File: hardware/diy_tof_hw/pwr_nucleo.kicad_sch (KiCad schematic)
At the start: 19 parts, among them IC1 TDC7200PWR, IC2 TDC7200PWR, J1 Conn_01x02_Pin, J2 Conn_01x03_Pin, J3 Conn_01x02_Pin, U1 NUCLEO-F042K6, X1 SG-5032CAN

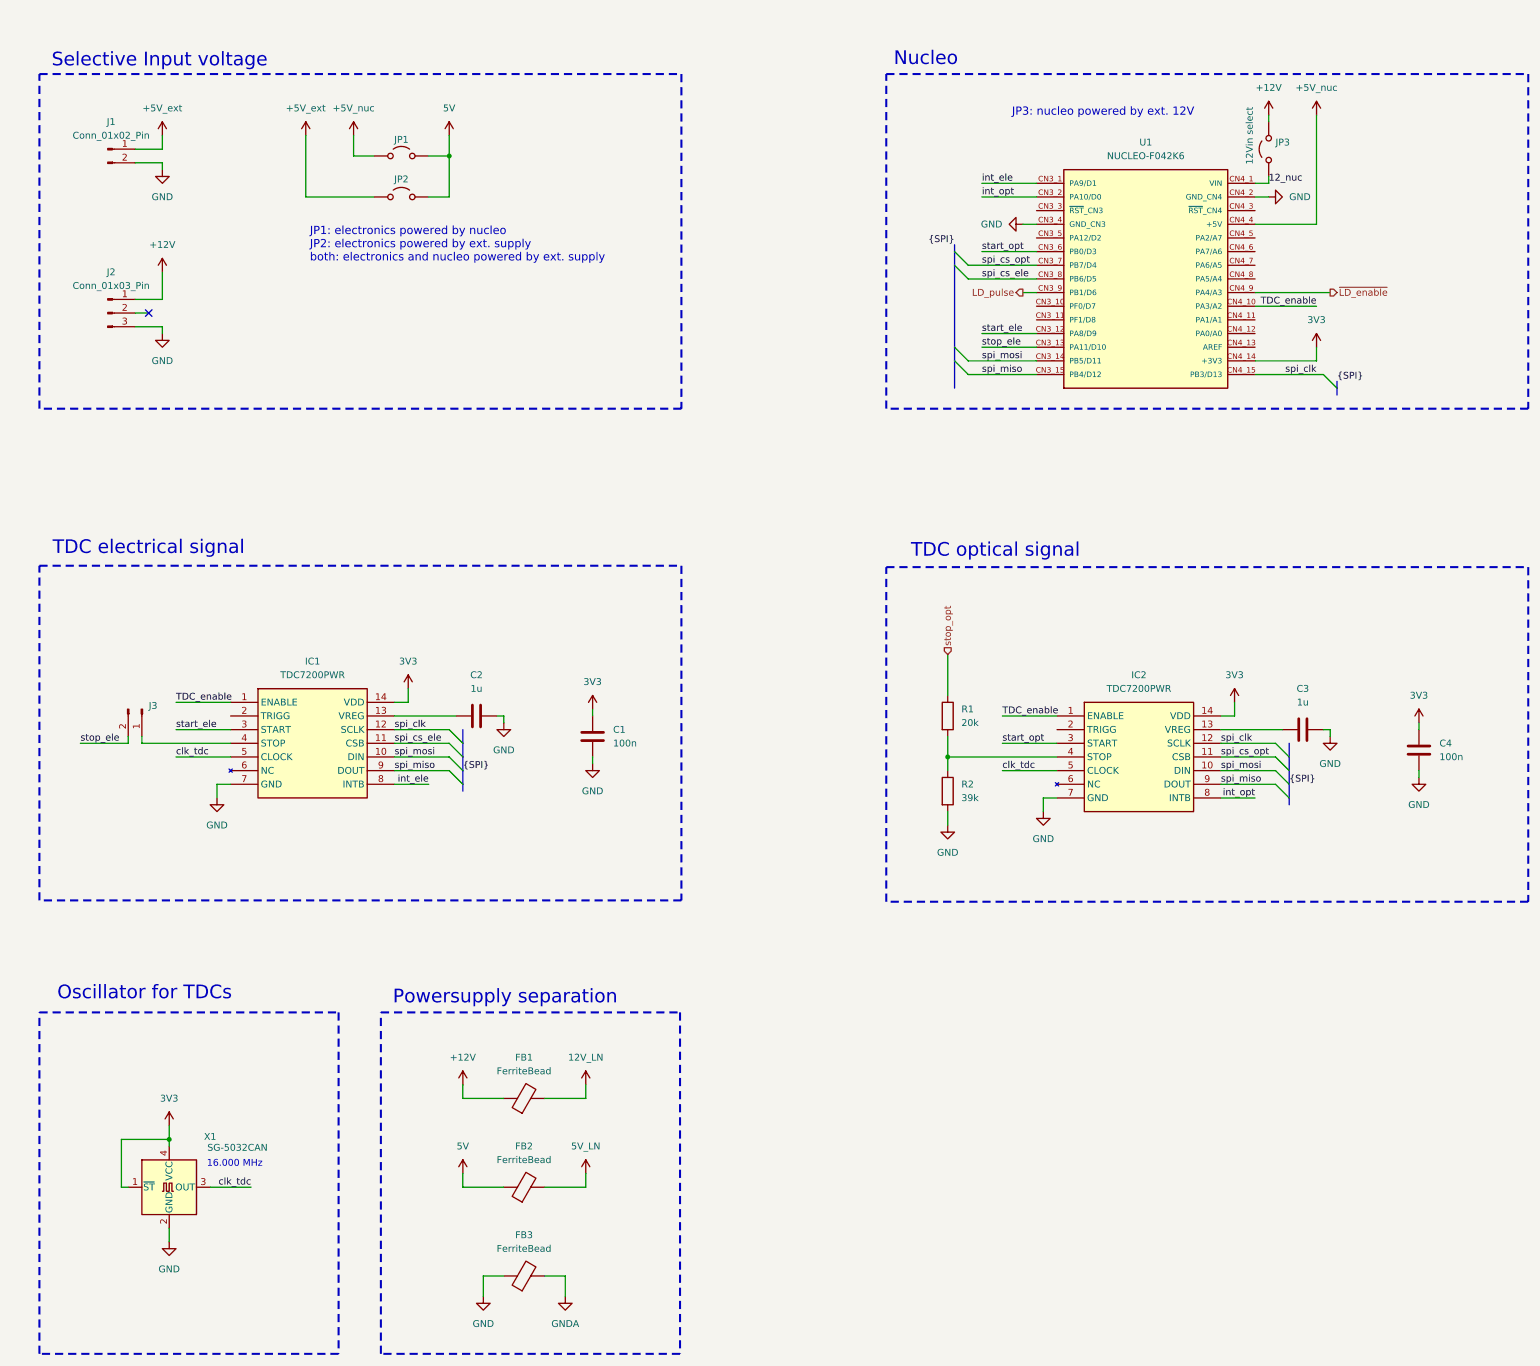
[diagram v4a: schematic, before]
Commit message: [hardware, firmware] various review findings  - added new signals TDC_opt/ele_enable  - fixed placement and appearance of the optics mount  - added switch for stop signal of the electrical TDC  - replaced "ground bead" with a 0R (in order to have a single clamping point for GND)  - added some additional decoupling caps for the laser driver  - reversed polarisation of the PD  - added a small resistor in between TIA and comparator  - adjusted RC to have higher capacitance and lower resistance  - cleaned up some labels / port names
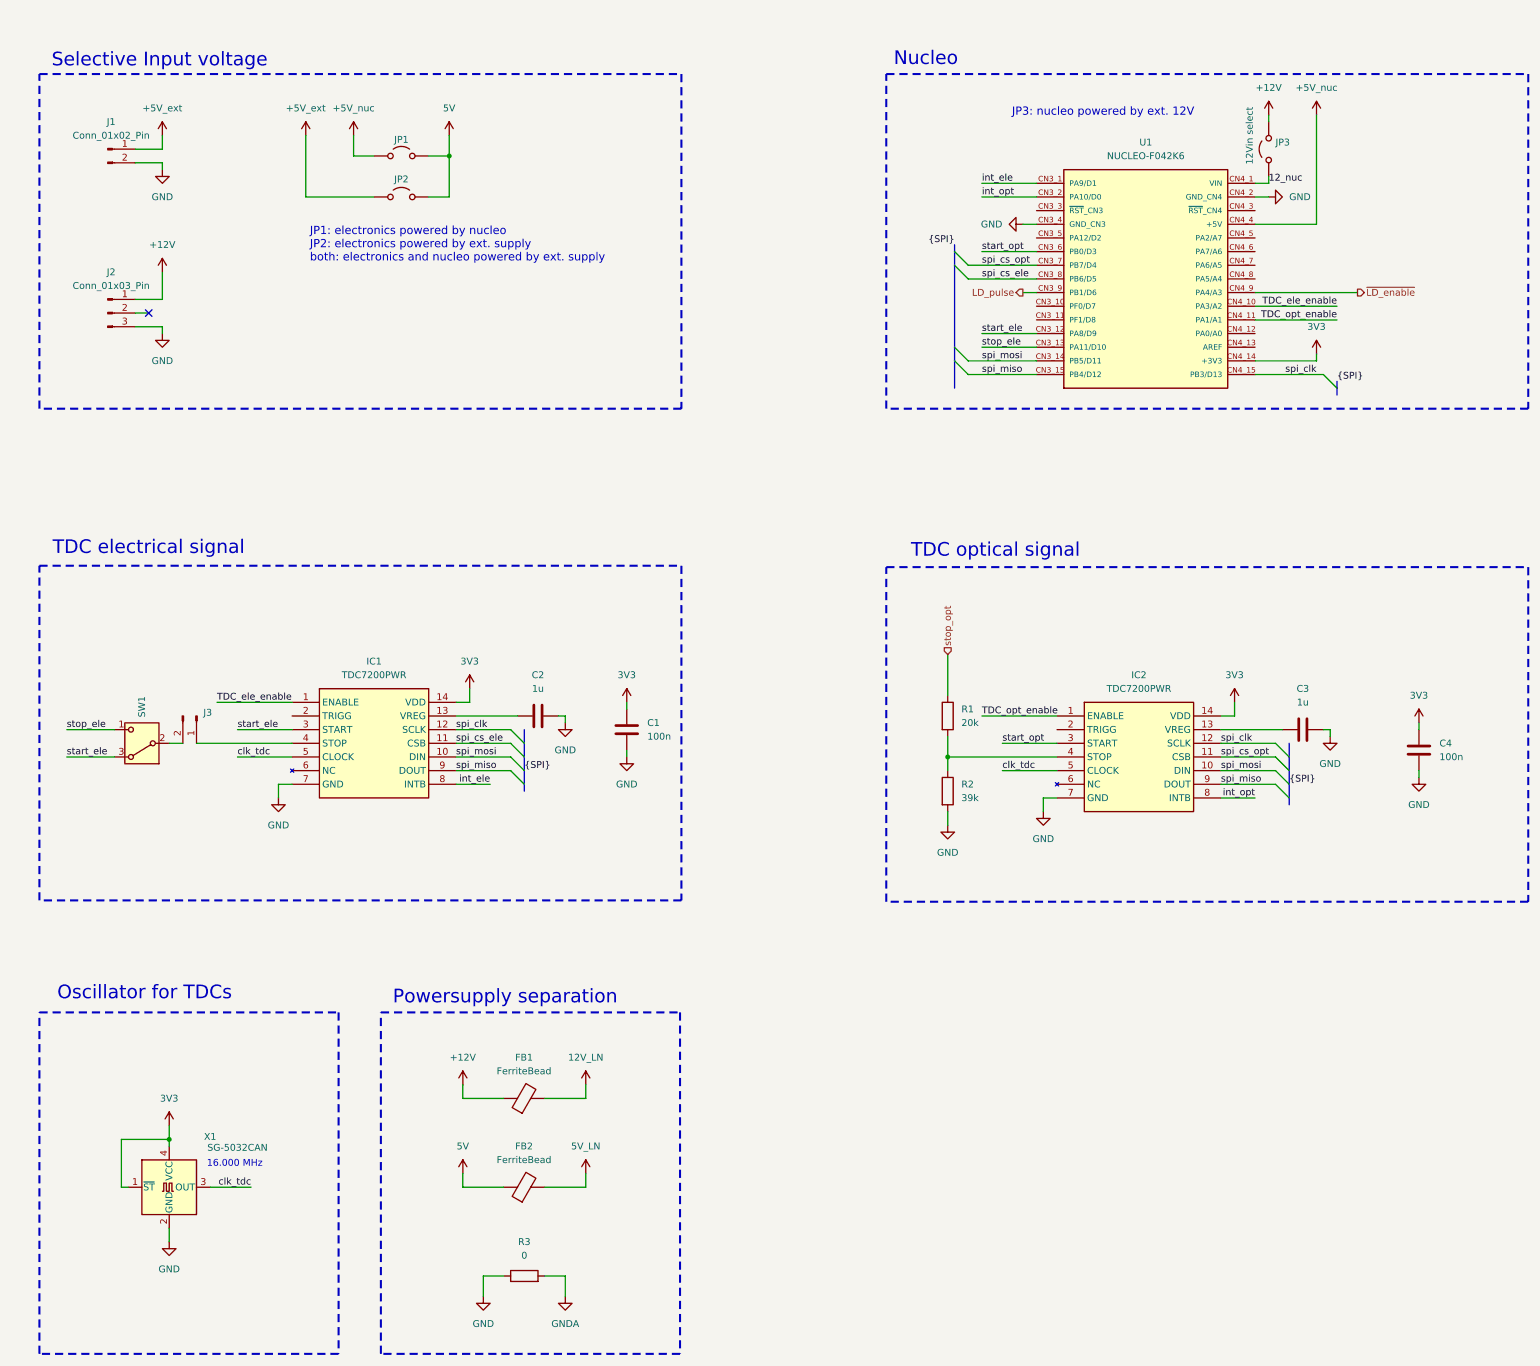
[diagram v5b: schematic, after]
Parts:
- removed FB3: FerriteBead, Inductor_SMD:L_0402_1005Metric_Pad0.77x0.64mm_HandSolder, symbol Device:FerriteBead
- added R3: 0, Resistor_SMD:R_0402_1005Metric_Pad0.72x0.64mm_HandSolder, symbol Device:R
- added SW1: SW_Nidec_CAS-120A1, Button_Switch_SMD:Nidec_Copal_CAS-120A, symbol Switch:SW_Nidec_CAS-120A1
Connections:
- net GND: now also R3.1
- net GNDA: now also R3.2
- net start_ele: now also SW1.3 (A)
- net stop_ele: now also SW1.1 (C); no longer J3.2 (Pin_2)
- net TDC_opt_enable: now reaches U1.CN4_11 (PA1/A1)
- net TDC_opt_enable: now also IC2.1 (ENABLE)
- net TDC_enable renamed TDC_ele_enable
- net TDC_ele_enable: no longer IC2.1 (ENABLE)
- new net: J3.2 (Pin_2), SW1.2 (B)
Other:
- moved on the sheet: C1, C2, IC1, J3
